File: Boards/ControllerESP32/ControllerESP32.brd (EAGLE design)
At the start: 157.1 x 99 mm, 14 parts

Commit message: cleaned up some stuff
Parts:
- removed BLE1: BLUEFRUITLE-SPI, Library:BLUEFRUITLE-SPI-SOCKET
- removed DS2: (no value), SparkFun-Connectors:1X03_LONGPADS
- removed SR1: SN74HC595N, SparkFun-IC-Logic:DIP16
- removed ST2: (no value), SparkFun-Connectors:1X04_LONGPADS
- removed STC2: POLOLU-MD09B, Library:POLOLU-MD09B
- added U$1: ESP32-DEV, IAD-Library:ESP32-DEV
- moved PW1 144.5 mm to (11.4, 10.2), turned to 180 degrees
- moved C3 127.9 mm to (11.4, 21.6)
- moved ST1 111.1 mm to (43.2, 10.2), turned to 0 degrees
- moved DS1 94.8 mm to (11.4, 35.6), turned to 270 degrees
- moved STC1 93.1 mm to (39.4, 26.7), turned to 270 degrees
- moved VR1 70.0 mm to (67.3, 30.5)
- moved C2 65.3 mm to (63.5, 11.4)
- moved C1 63.7 mm to (71.1, 11.4), turned to 270 degrees
- moved MCU1 32.5 mm to (33.0, 55.9), turned to 0 degrees
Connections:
- net ST1_BLUE renamed ST_BLUE
- net ST1_GREEN renamed ST_GREEN
- net ST1_RED renamed ST_RED
- net ST1_YELLOW renamed ST_YELLOW
- removed net BLE_CS: BLE1.4, MCU1.16
- removed net BLE_IRQ: BLE1.5, MCU1.15
- removed net BLE_MISO: BLE1.2, MCU1.19
- removed net BLE_MOSI: BLE1.3, MCU1.17
- removed net BLE_SCK: BLE1.1, MCU1.18
- removed net DS2_SIG: DS2.3, MCU1.3
- removed net N$6: STC2.5, STC2.6
- removed net SR1_RCK: MCU1.9, SR1.12
- removed net SR1_SCK: MCU1.10, SR1.11
- removed net SR1_SER: MCU1.21, MCU1.8, SR1.14
- removed net ST2_BLUE: ST2.1, STC2.11
- removed net ST2_GREEN: ST2.4, STC2.14
- removed net ST2_RED: ST2.3, STC2.13
- removed net ST2_YELLOW: ST2.2, STC2.12
- removed net STC1_DIR: MCU1.14, STC1.8
- removed net STC1_EN: SR1.7, STC1.1
- removed net STC1_MS1: SR1.6, STC1.2
- removed net STC1_MS2: SR1.5, STC1.3
- removed net STC1_MS3: SR1.4, STC1.4
- removed net STC1_STEP: MCU1.13, STC1.7
- removed net STC2_DIR: MCU1.11, STC2.8
- removed net STC2_EN: SR1.3, STC2.1
- removed net STC2_MS1: SR1.2, STC2.2
- removed net STC2_MS2: SR1.1, STC2.3
- removed net STC2_MS3: SR1.15, STC2.4
- removed net STC2_STEP: MCU1.12, STC2.7
- new net STC_DIR: MCU1.9, STC1.8
- new net STC_EN: MCU1.14, STC1.1
- new net STC_MS1: MCU1.13, STC1.2
- new net STC_MS2: MCU1.12, STC1.3
- new net STC_MS3: MCU1.11, STC1.4
- new net STC_STEP: MCU1.10, STC1.7
- net 12V: no longer STC2.16
- net 3V: now also DS1.3; no longer BLE1.9, DS1.1, DS2.1, SR1.10, SR1.16, STC2.10
- net DS1_SIG: now also DS1.2; no longer DS1.3
- net GND: now also DS1.1; no longer BLE1.8, DS1.2, DS2.2, SR1.13, SR1.8, STC2.15, STC2.9
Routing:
- net 3V: track 306.3 -> 0.00 mm
- net 5V: track 216.8 -> 0.00 mm
- net 12V: track 93.6 -> 0.00 mm
- net STC1_MS2: track 65.5 -> 0.00 mm
- net DS2_SIG: track 54.0 -> 0.00 mm
- net SR1_SER: track 49.7 -> 0.00 mm
- net DS1_SIG: track 42.9 -> 0.00 mm
- net STC1_MS1: track 42.7 -> 0.00 mm
- net STC1_EN: track 42.7 -> 0.00 mm
- net STC2_MS3: track 42.4 -> 0.00 mm
- net STC1_MS3: track 41.6 -> 0.00 mm
- net STC2_MS1: track 33.1 -> 0.00 mm
- net STC2_EN: track 32.7 -> 0.00 mm
- net STC2_MS2: track 32.2 -> 0.00 mm
- net BLE_MISO: track 31.6 -> 0.00 mm
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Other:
- board size 157.1 x 99 mm -> 81.3 x 77.1 mm

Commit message: finished esp32 based board
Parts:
- removed MCU1: MKR1000, Library:MKR1000-SOCKET
- moved U$1 89.2 mm to (38.1, 57.1), flipped to the bottom
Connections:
- net 3V: now also U$1.1; no longer MCU1.26
- net 5V: now also U$1.19; no longer MCU1.27
- net DS1_SIG: now also U$1.15; no longer MCU1.2
- net GND: now also U$1.14, U$1.32, U$1.38; no longer MCU1.25
- net STC_DIR: now also U$1.8; no longer MCU1.9
- net STC_EN: now also U$1.13; no longer MCU1.14
- net STC_MS1: now also U$1.12; no longer MCU1.13
- net STC_MS2: now also U$1.11; no longer MCU1.12
- net STC_MS3: now also U$1.10; no longer MCU1.11
- net STC_STEP: now also U$1.9; no longer MCU1.10
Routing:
- net 12V: track 0.00 -> 104.8 mm
- net 5V: track 0.00 -> 91.9 mm
- net 3V: track 0.00 -> 67.5 mm
- net DS1_SIG: track 0.00 -> 25.3 mm
- net STC_DIR: track 0.00 -> 13.6 mm
- net STC_STEP: track 0.00 -> 13.5 mm
- net STC_EN: track 0.00 -> 12.8 mm
- net ST_GREEN: track 0.00 -> 12.4 mm
- net ST_BLUE: track 0.00 -> 12.3 mm
- net STC_MS2: track 0.00 -> 11.8 mm
- net STC_MS3: track 0.00 -> 11.7 mm
- net STC_MS1: track 0.00 -> 11.4 mm
- net ST_YELLOW: track 0.00 -> 10.5 mm
- net ST_RED: track 0.00 -> 10.2 mm
- net N$1: track 0.00 -> 2.55 mm
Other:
- board size 81.3 x 77.1 mm -> 81.3 x 79.7 mm

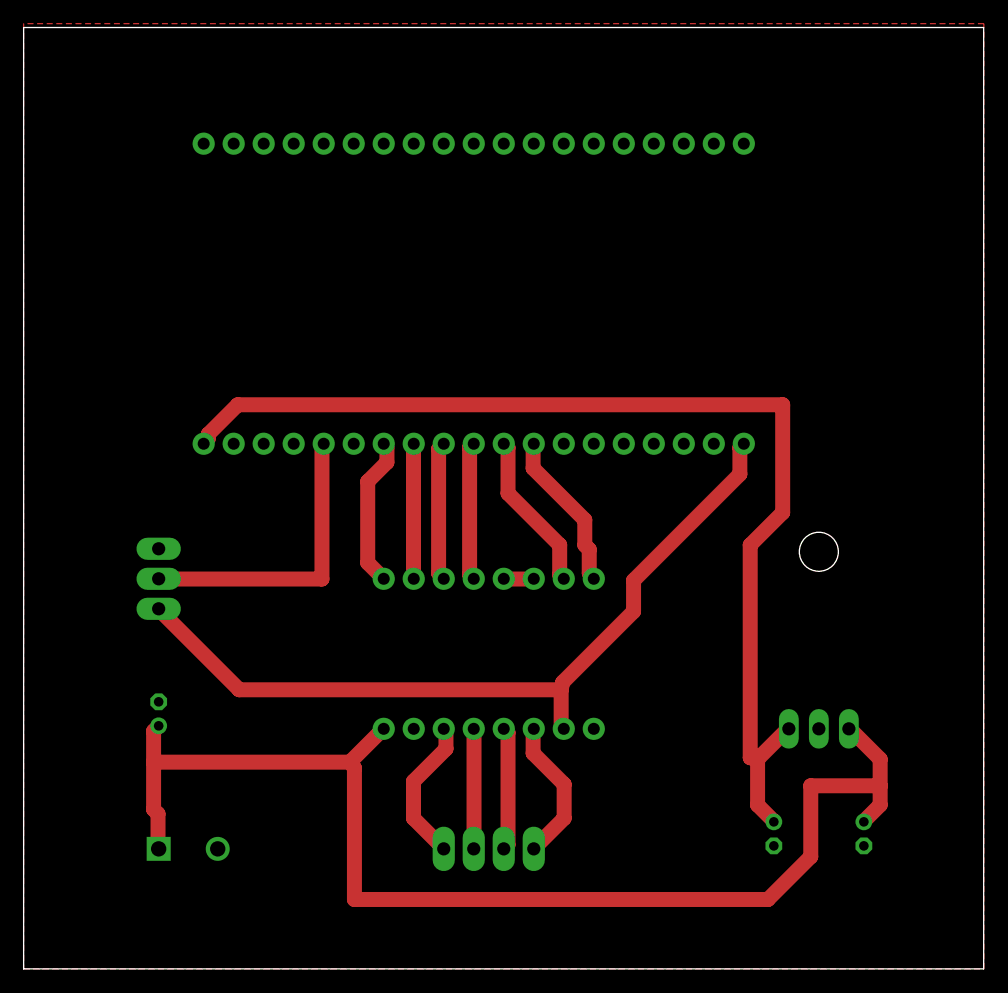
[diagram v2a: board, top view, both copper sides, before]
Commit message: finish esp32 based controller
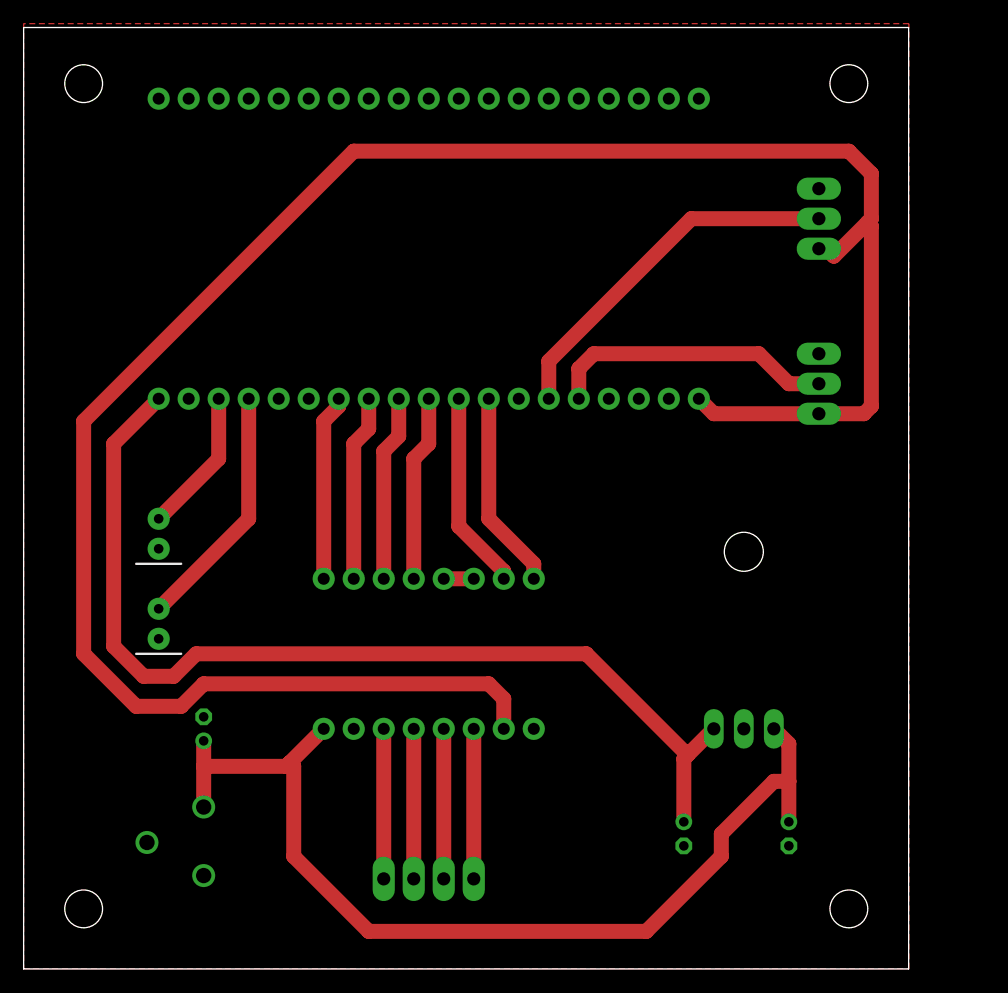
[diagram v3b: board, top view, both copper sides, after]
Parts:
- removed PW1: (no value), SparkFun-Connectors:SCREWTERMINAL-5MM-2
- removed U$1: ESP32-DEV, IAD-Library:ESP32-DEV
- added D1: GREEN (CONN), SparkFun-LED:LED_5MM
- added D2: RED (PWR), SparkFun-LED:LED_5MM
- added DS2: (no value), SparkFun-Connectors:1X03_LONGPADS
- added J1: POWER_JACKPTH_BREAD, SparkFun-Connectors:POWER_JACK_PTH_BREAD
- added MCU1: ESP32-DEV, IAD-Library:ESP32-DEV
- moved DS1 58.3 mm to (67.3, 52.1)
- moved C2 7.62 mm to (55.9, 11.4)
- moved C1 6.35 mm to (64.8, 11.4)
- moved VR1 6.35 mm to (61.0, 30.5)
- moved ST1 5.68 mm to (38.1, 7.62)
- moved STC1 5.08 mm to (34.3, 26.7)
- moved C3 4.02 mm to (15.2, 20.3)
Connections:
- new net DS2_SIG: DS2.2, MCU1.6
- new net LED1: D1.A, MCU1.16
- new net LED2: D2.A, MCU1.17
- net 12V: now also J1.PWR; no longer PW1.1
- net 3V: now also DS2.3, MCU1.1; no longer U$1.1
- net 5V: now also MCU1.19; no longer U$1.19
- net DS1_SIG: now also MCU1.5; no longer U$1.15
- net GND: now also D1.K, D2.K, DS2.1, J1.GND, MCU1.14, MCU1.32, MCU1.38; no longer PW1.2, U$1.14, U$1.32, U$1.38
- net STC_DIR: now also MCU1.8; no longer U$1.8
- net STC_EN: now also MCU1.13; no longer U$1.13
- net STC_MS1: now also MCU1.12; no longer U$1.12
- net STC_MS2: now also MCU1.11; no longer U$1.11
- net STC_MS3: now also MCU1.10; no longer U$1.10
- net STC_STEP: now also MCU1.9; no longer U$1.9
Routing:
- net 3V: track 67.5 -> 178.8 mm
- net DS2_SIG: track 0.00 -> 31.0 mm
- net LED1: track 0.00 -> 20.9 mm
- net 12V: track 104.8 -> 84.5 mm
- net LED2: track 0.00 -> 12.3 mm
- net 5V: track 91.9 -> 85.4 mm
- net STC_MS1: track 11.4 -> 15.8 mm
- net STC_MS3: track 11.7 -> 15.8 mm
- net STC_MS2: track 11.8 -> 15.8 mm
- net STC_STEP: track 13.5 -> 16.8 mm
- net STC_DIR: track 13.6 -> 16.8 mm
- net STC_EN: track 12.8 -> 15.8 mm
- net ST_RED: track 10.2 -> 12.7 mm
- net ST_YELLOW: track 10.5 -> 12.7 mm
- net DS1_SIG: track 25.3 -> 24.4 mm
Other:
- board size 81.3 x 79.7 mm -> 74.9 x 79.7 mm

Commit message: finished esp32 board based board
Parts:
- added U$1, U$2, U$3, U$4: (no value), SparkFun-Hardware:STAND-OFF
- moved DS2 58.9 mm to (8.89, 58.4), flipped to the top
- moved DS1 58.6 mm to (8.89, 47.0), flipped to the top
- moved D1 48.9 mm to (59.7, 21.6), flipped to the top
- moved D2 48.7 mm to (59.7, 30.5), flipped to the top
- moved VR1 46.0 mm to (15.2, 25.4), flipped to the top
- moved J1 44.4 mm to (59.7, 0.00), flipped to the top
- moved C1 41.9 mm to (22.9, 10.2), flipped to the top
- moved C3 37.0 mm to (50.8, 10.2), flipped to the top
- moved C2 25.4 mm to (30.5, 10.2), flipped to the top
- moved MCU1 10.9 mm to (40.6, 52.1), flipped to the top
- moved STC1 6.48 mm to (40.6, 25.4), flipped to the top
- moved ST1 1.80 mm to (36.8, 8.89), flipped to the top
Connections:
- net LED1: now also MCU1.31; no longer MCU1.16
- net LED2: now also MCU1.30; no longer MCU1.17
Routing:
- net 3V: track 178.8 -> 0.00 mm
- net LED1: track 20.9 -> 63.5 mm
- net LED2: track 12.3 -> 52.9 mm
- net 5V: track 85.4 -> 66.2 mm
- net 12V: track 84.5 -> 69.3 mm
- net STC_DIR: track 16.8 -> 9.39 mm
- net STC_STEP: track 16.8 -> 9.42 mm
- net STC_EN: track 15.8 -> 8.59 mm
- net STC_MS1: track 15.8 -> 8.86 mm
- net STC_MS2: track 15.8 -> 8.86 mm
- net STC_MS3: track 15.8 -> 8.86 mm
- net DS1_SIG: track 24.4 -> 21.3 mm
- net ST_BLUE: track 12.7 -> 10.7 mm
- net ST_YELLOW: track 12.7 -> 10.7 mm
- net ST_RED: track 12.7 -> 10.7 mm
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- added copper zone on layer 1, net 3V
- added copper zone on layer 16, net GND
- removed copper zone on layer 1, net GND
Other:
- board size 74.9 x 79.7 mm -> 74.9 x 74.6 mm
